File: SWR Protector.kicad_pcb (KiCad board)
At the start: 2 copper layers, 82.7 x 56.6 mm, 28 parts, among them J1 Barrel_Jack, J2 Barrel_Jack, J3 transceiver, J4 antenna, J5 header, K2 ATX209, Q1 2N3904, T1 1:12, T2 1:12, U1 LM78L05_TO92, U2 LM358

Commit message: checkpoint changes working on V2.0
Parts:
- moved J1 1.63 mm to (182.6, 124.5)
- moved J2 1.02 mm to (127.3, 124.5)
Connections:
- U2 pad 8: +5V -> +12V
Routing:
- net +12V: track 54.2 -> 72.9 mm
- net +5V: track 124.4 -> 108.5 mm
- net GND: vias 74 -> 0

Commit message: checkpoint changes working on V2.0
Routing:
- net +5V: track 108.5 -> 117.7 mm, vias 2 -> 1
- net Net-(D4-K): track 47.2 -> 48.6 mm
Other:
- board text added: "SWR Protector v1.1"
- board text removed: "SWR Protector v1.0"

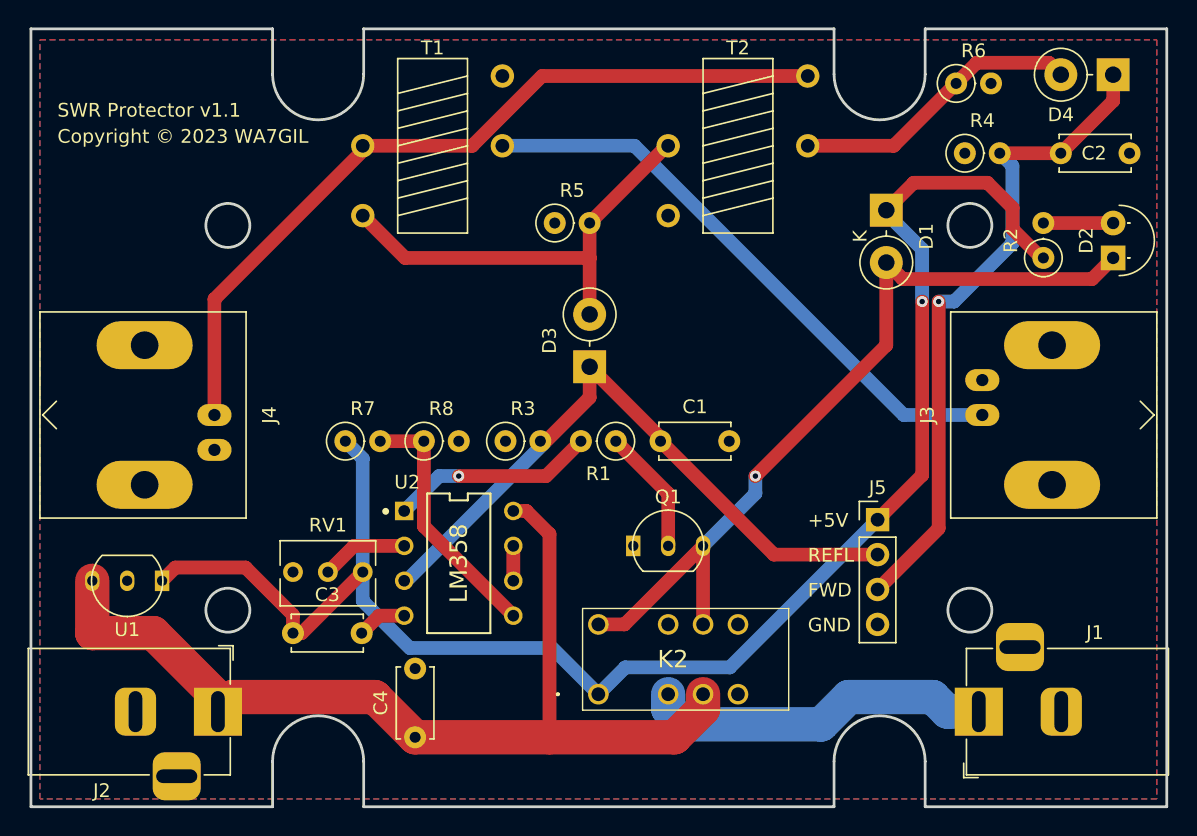
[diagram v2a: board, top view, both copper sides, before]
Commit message: completed everything on the list of requested changes in V2-Changelog.txt.  Passes DRC, but we get warnings for things like silkscreen off the edge of the board (deliberate, for the power connectors).  Needs a hard squint, then send it off to the fab.
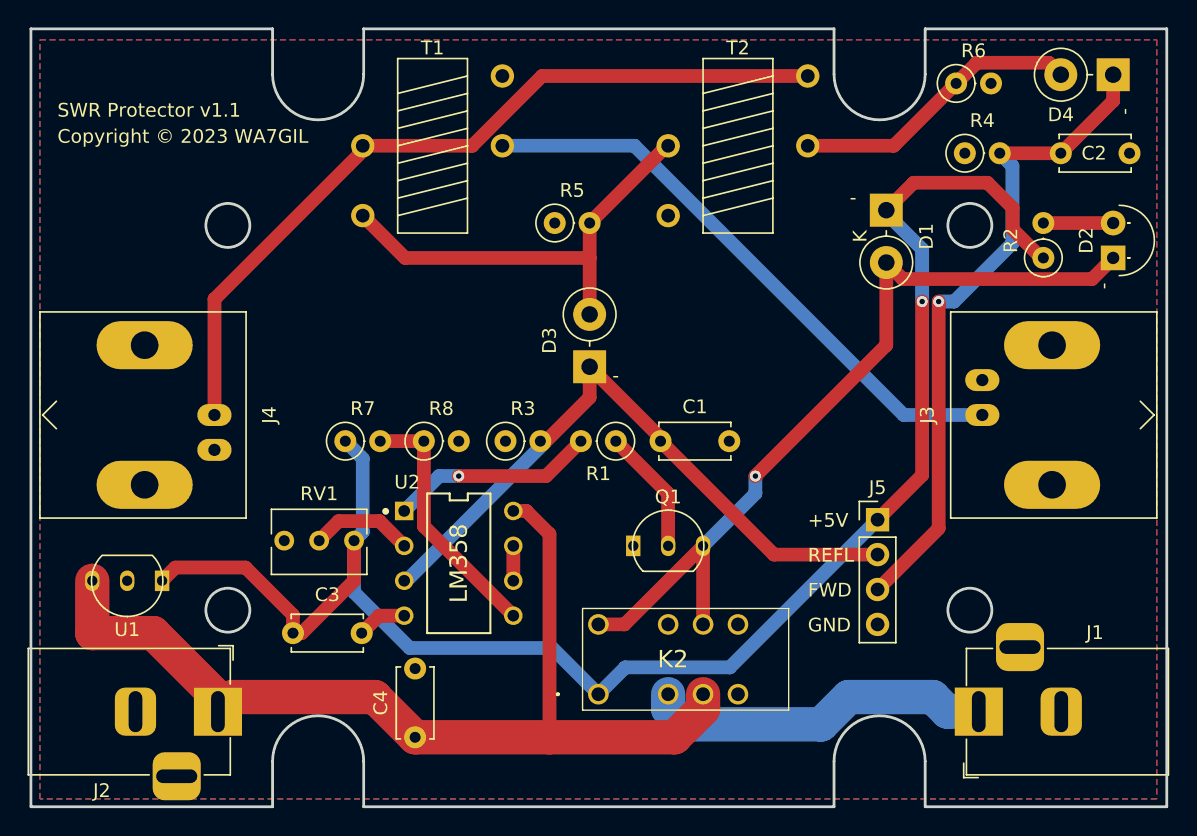
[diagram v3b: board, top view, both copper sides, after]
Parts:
- moved RV1 2.37 mm to (137.2, 112.0)
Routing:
- net +5V: track 117.7 -> 120.2 mm
- net Net-(U2A--): track 6.34 -> 7.52 mm
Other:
- board text added: "-"
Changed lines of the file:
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@@
   )
   (footprint "Potentiometer_THT:Potentiometer_Bourns_3266Y_Vertical" (layer "F.Cu")
-    (at 137.795 114.3)
+    (at 137.16 112.014)
     (descr "Potentiometer, vertical, Bourns 3266Y, https://www.bourns.com/docs/Product-Datasheets/3266.pdf")
     (tags "Potentiometer vertical Bourns 3266Y")
@@
     (fp_line (start 0.935 0.496) (end 0.935 2.46)
       (stroke (width 0.12) (type solid)) (layer "F.SilkS"))
-    (fp_line (start -6.15 -2.45) (end -6.15 2.6)
-      (stroke (width 0.05) (type solid)) (layer "F.CrtYd"))
-    (fp_line (start -6.15 2.6) (end 1.1 2.6)
-      (stroke (width 0.05) (type solid)) (layer "F.CrtYd"))
-    (fp_line (start 1.1 -2.45) (end -6.15 -2.45)
-      (stroke (width 0.05) (type solid)) (layer "F.CrtYd"))
-    (fp_line (start 1.1 2.6) (end 1.1 -2.45)
+    (fp_line (start -7 -4.5) (end -7 4.5)
+      (stroke (width 0.05) (type solid)) (layer "F.CrtYd"))
+    (fp_line (start -7 4.5) (end 2 4.5)
+      (stroke (width 0.05) (type solid)) (layer "F.CrtYd"))
+    (fp_line (start 2 -4.5) (end -7 -4.5)
+      (stroke (width 0.05) (type solid)) (layer "F.CrtYd"))
+    (fp_line (start 2 4.5) (end 2 -4.5)
       (stroke (width 0.05) (type solid)) (layer "F.CrtYd"))
     (fp_line (start -5.895 -2.16) (end -5.895 2.34)
@@
     (effects (font (size 1 1) (thickness 0.15)) (justify left bottom))
   )
+  (gr_text "-" (at 193.802 81.026 90) (layer "F.SilkS")
+    (effects (font (size 1 1) (thickness 0.15)) (justify left bottom))
+  )
+  (gr_text "-" (at 192.278 93.726 90) (layer "F.SilkS")
+    (effects (font (size 1 1) (thickness 0.15)) (justify left bottom))
+  )
+  (gr_text "-" (at 173.228 87.63) (layer "F.SilkS")
+    (effects (font (size 1 1) (thickness 0.15)) (justify left bottom))
+  )
   (gr_text "REFL" (at 170.18 113.665) (layer "F.SilkS")
     (effects (font (size 1 1) (thickness 0.15)) (justify left bottom))
@@
   )
   (gr_text "SWR Protector v1.1" (at 115.57 81.28) (layer "F.SilkS")
+    (effects (font (size 1 1) (thickness 0.15)) (justify left bottom))
+  )
+  (gr_text "-" (at 155.956 100.584) (layer "F.SilkS")
     (effects (font (size 1 1) (thickness 0.15)) (justify left bottom))
   )
@@
   (segment (start 185.076693 84.746693) (end 185.076693 90.362295) (width 1) (layer "B.Cu") (net 3))
   (segment (start 184.15 83.82) (end 185.076693 84.746693) (width 1) (layer "B.Cu") (net 3))
-  (segment (start 132.715 118.745) (end 133.35 118.745) (width 1) (layer "F.Cu") (net 4))
   (segment (start 185.08705 87.797784) (end 183.261593 85.972327) (width 1) (layer "F.Cu") (net 4))
   (segment (start 132.715 117.425734) (end 129.261593 113.972327) (width 1) (layer "F.Cu") (net 4))
+  (segment (start 132.715 118.745) (end 133.35 118.745) (width 1) (layer "F.Cu") (net 4))
   (segment (start 124.152673 113.972327) (end 123.19 114.935) (width 1) (layer "F.Cu") (net 4))
+  (segment (start 133.35 118.745) (end 137.16 114.935) (width 1) (layer "F.Cu") (net 4))
   (segment (start 185.08705 89.344041) (end 185.08705 87.797784) (width 1) (layer "F.Cu") (net 4))
   (segment (start 177.887673 85.972327) (end 175.895 87.965) (width 1) (layer "F.Cu") (net 4))
   (segment (start 187.325 91.44) (end 187.183009 91.44) (width 1) (layer "F.Cu") (net 4))
-  (segment (start 133.35 118.745) (end 137.795 114.3) (width 1) (layer "F.Cu") (net 4))
   (segment (start 178.505 107.245) (end 178.505 94.615) (width 1) (layer "F.Cu") (net 4))
   (segment (start 187.183009 91.44) (end 185.08705 89.344041) (width 1) (layer "F.Cu") (net 4))
@@
   (segment (start 183.261593 85.972327) (end 177.887673 85.972327) (width 1) (layer "F.Cu") (net 4))
   (segment (start 129.261593 113.972327) (end 124.152673 113.972327) (width 1) (layer "F.Cu") (net 4))
+  (segment (start 137.16 114.935) (end 137.16 112.014) (width 1) (layer "F.Cu") (net 4))
   (via (at 178.505 94.615) (size 0.8) (drill 0.4) (layers "F.Cu" "B.Cu") (net 4))
+  (segment (start 141.215456 119.825) (end 151.575 119.825) (width 1) (layer "B.Cu") (net 4))
   (segment (start 175.895 88.195) (end 178.505 90.805) (width 1) (layer "B.Cu") (net 4))
-  (segment (start 141.215456 119.825) (end 151.575 119.825) (width 1) (layer "B.Cu") (net 4))
   (segment (start 175.26 110.49) (end 164.51 121.24) (width 1) (layer "B.Cu") (net 4))
   (segment (start 178.505 94.615) (end 178.505 90.805) (width 1) (layer "B.Cu") (net 4))
-  (segment (start 137.795 114.3) (end 137.795 116.404544) (width 1) (layer "B.Cu") (net 4))
+  (segment (start 151.575 119.825) (end 154.94 123.19) (width 1) (layer "B.Cu") (net 4))
   (segment (start 156.89 121.24) (end 154.94 123.19) (width 1) (layer "B.Cu") (net 4))
   (segment (start 164.51 121.24) (end 156.89 121.24) (width 1) (layer "B.Cu") (net 4))
+  (segment (start 137.795 111.379) (end 137.795 106.045) (width 1) (layer "B.Cu") (net 4))
+  (segment (start 175.895 87.965) (end 175.895 88.195) (width 1) (layer "B.Cu") (net 4))
+  (segment (start 137.16 112.014) (end 137.795 111.379) (width 1) (layer "B.Cu") (net 4))
+  (segment (start 137.16 112.014) (end 137.16 115.769544) (width 1) (layer "B.Cu") (net 4))
+  (segment (start 137.16 115.769544) (end 141.215456 119.825) (width 1) (layer "B.Cu") (net 4))
   (segment (start 137.795 106.045) (end 136.525 104.775) (width 1) (layer "B.Cu") (net 4))
-  (segment (start 175.895 87.965) (end 175.895 88.195) (width 1) (layer "B.Cu") (net 4))
-  (segment (start 137.795 116.404544) (end 141.215456 119.825) (width 1) (layer "B.Cu") (net 4))
-  (segment (start 151.575 119.825) (end 154.94 123.19) (width 1) (layer "B.Cu") (net 4))
-  (segment (start 137.795 114.3) (end 137.795 106.045) (width 1) (layer "B.Cu") (net 4))
   (segment (start 122.555 118.745) (end 118.11 118.745) (width 2.5) (layer "F.Cu") (net 5))
   (segment (start 151.384 111.534406) (end 151.384 126.325) (width 1) (layer "F.Cu") (net 5))
@@
   (segment (start 142.24 104.775) (end 139.065 104.775) (width 1) (layer "F.Cu") (net 17))
   (segment (start 142.24 110.965) (end 148.75 117.475) (width 1) (layer "F.Cu") (net 17))
-  (segment (start 140.81 112.395) (end 137.16 112.395) (width 1) (layer "F.Cu") (net 18))
-  (segment (start 137.16 112.395) (end 135.255 114.3) (width 1) (layer "F.Cu") (net 18))
+  (segment (start 139.009 110.594) (end 140.81 112.395) (width 1) (layer "F.Cu") (net 18))
+  (segment (start 136.04 110.594) (end 139.009 110.594) (width 1) (layer "F.Cu") (net 18))
+  (segment (start 134.62 112.014) (end 136.04 110.594) (width 1) (layer "F.Cu") (net 18))
   (segment (start 148.75 114.935) (end 148.75 112.395) (width 1) (layer "F.Cu") (net 19))
   (zone (net 2) (net_name "GND") (layer "F.Cu") (hatch edge 0.5)

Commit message: v1.2 - added pins 2 & 3 from LM358 to header
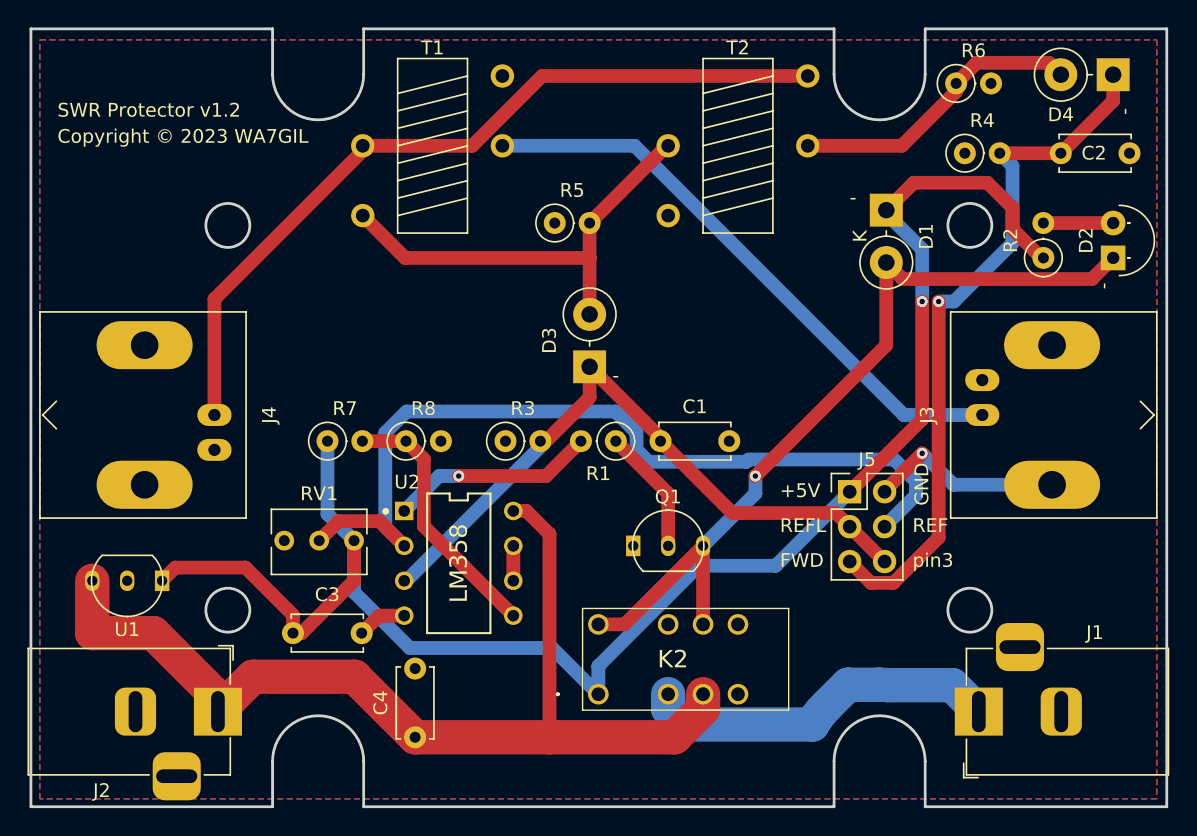
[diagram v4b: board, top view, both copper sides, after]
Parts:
- J5: value header -> Conn_02x03; footprint Connector_PinHeader_2.54mm:PinHeader_1x04_P2.54mm_Vertical -> Connector_PinHeader_2.54mm:PinHeader_2x03_P2.54mm_Vertical
- moved J5 2.87 mm to (173.2, 108.5)
- moved R7 1.30 mm to (135.2, 104.8)
- moved R8 1.30 mm to (140.9, 104.8)
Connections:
- J5 pad 2: Net-(D3-K) -> GND
- J5 pad 3: Net-(D4-K) -> Net-(D3-K)
- J5 pad 4: GND -> Net-(J5-Pin_4)
- RV1 pad 2: Net-(U2A--) -> Net-(J5-Pin_4)
- U2 pad 2: Net-(U2A--) -> Net-(J5-Pin_4)
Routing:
- net Net-(J5-Pin_4): track 0.00 -> 62.8 mm
- net GND: track 3.62 -> 18.0 mm, vias 0 -> 1
- net Net-(U2A--): track 7.52 -> 0.00 mm
- net Net-(D4-K): track 48.6 -> 51.5 mm
- net +12V: track 72.9 -> 74.1 mm
- net +5V: track 120.2 -> 119.0 mm
- net Net-(K2-NC_1): track 25.4 -> 26.3 mm
- net Net-(D3-K): track 48.0 -> 48.7 mm
- net Net-(U2B-+): track 18.6 -> 19.1 mm
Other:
- board text added: "REF"
- board text added: "SWR Protector v1.2"
- board text added: "pin3"
- board text removed: "SWR Protector v1.1"

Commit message: checkpoint changes made late satuday that i cannot remember what i did
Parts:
- renumbered C4 to C2, C2 to C4, D3 to D1, D4 to D2, D2 to D3, D1 to D4, J2 to J1, J4 to J2, J5 to J3, J3 to J4, J1 to J5, K2 to K1, R5 to R1, R3 to R2, R4 to R3, R6 to R4, R1 to R5, R2 to R6

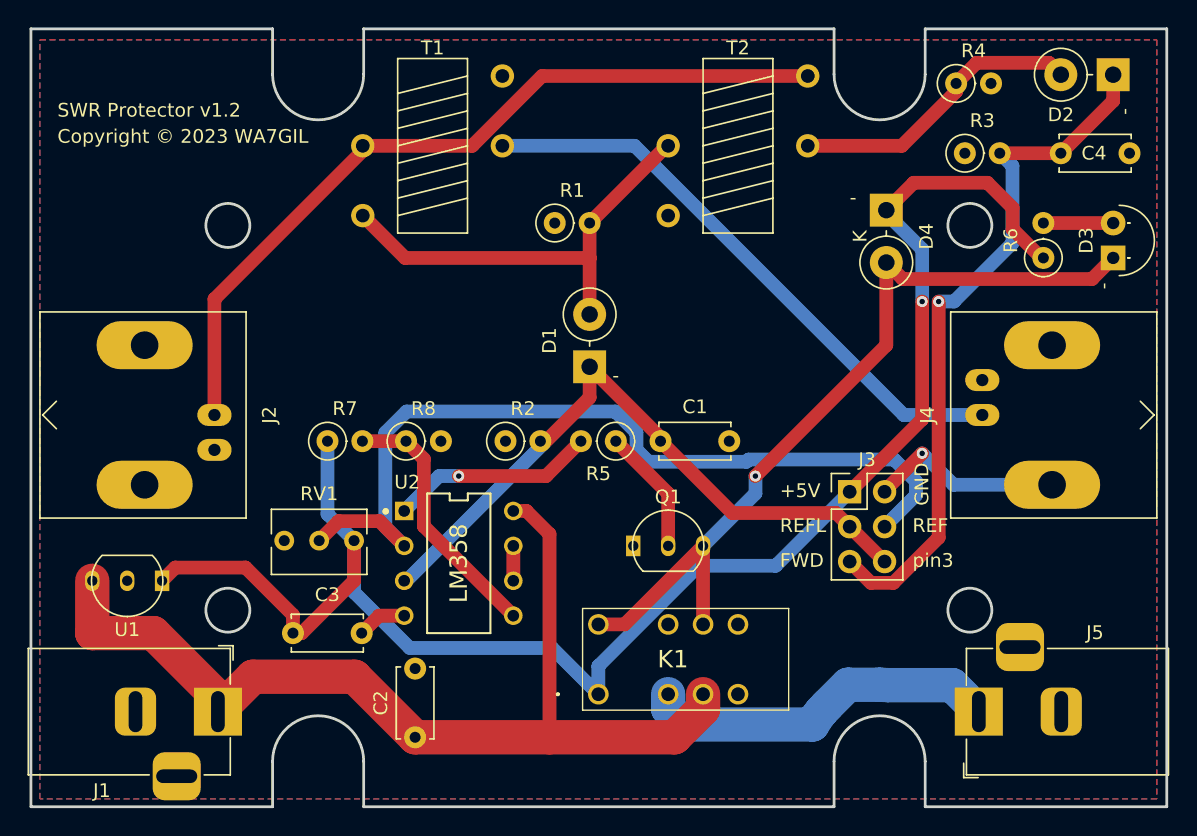
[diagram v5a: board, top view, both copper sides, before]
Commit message: Removed pin 6 on header.  Fine tune footprint for Q1. Realizing pin 6 on header just duplicated the VReflected voltage already on pin 3, I made pin 6 NC. Fiddled with footprint for Q1 to try to remove "Silkscreen clipped by solder mask" warnings.
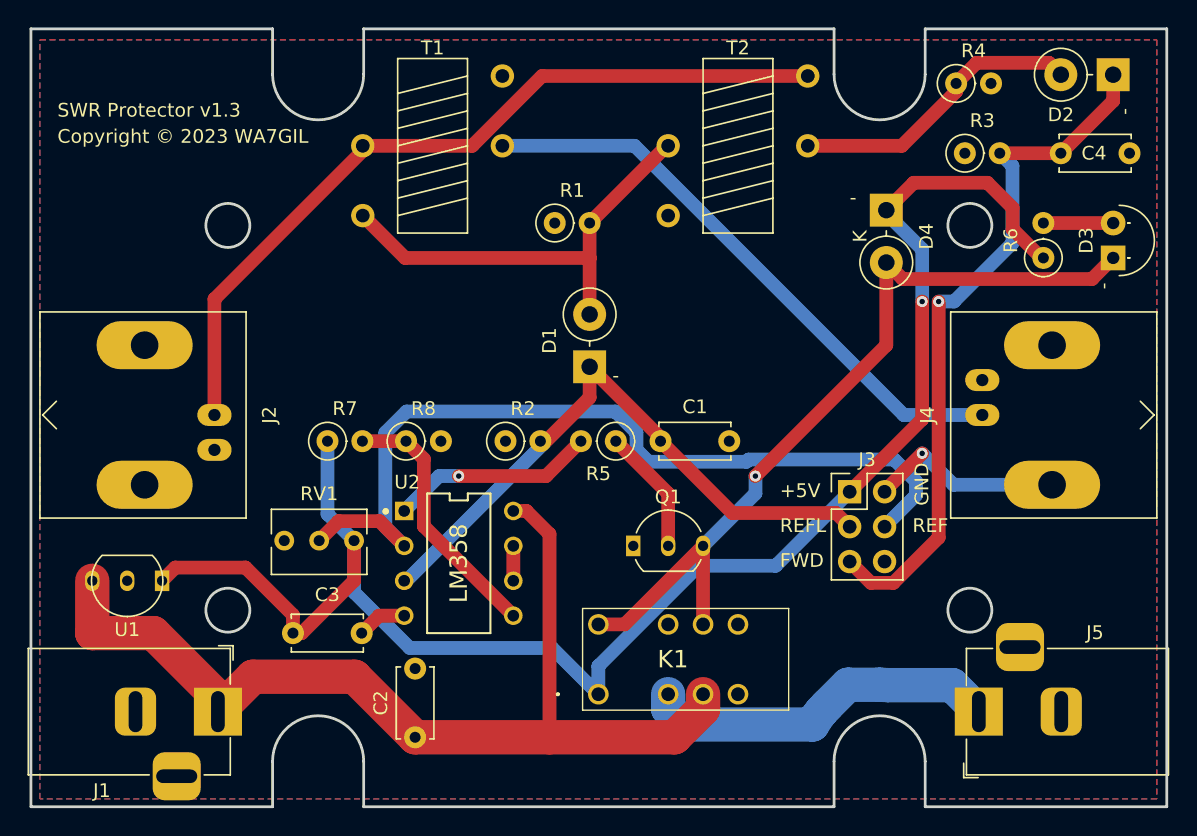
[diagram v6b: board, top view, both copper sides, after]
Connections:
- J3 pad 6: Net-(D1-K) -> unconnected-(J3-Pin_6-Pad6)
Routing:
- net Net-(D1-K): track 48.7 -> 45.2 mm
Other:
- board text added: "SWR Protector v1.3"
- board text removed: "SWR Protector v1.2"
- board text removed: "pin3"
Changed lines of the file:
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@@
   (title_block
     (title "SWR Protector WA7GIL")
-    (date "2023-05-27")
-    (rev "v1.2")
+    (date "2023-05-28")
+    (rev "v1.3")
   )
   (layers
@@
   (net 18 "Net-(R5-Pad2)")
   (net 19 "Net-(U2B--)")
+  (net 20 "unconnected-(J3-Pin_6-Pad6)")
   (footprint "Capacitor_THT:C_Disc_D5.0mm_W2.5mm_P5.00mm" (layer "F.Cu")
     (at 188.595 83.82)
@@
     (fp_line (start -0.53 1.85) (end 3.07 1.85)
       (stroke (width 0.12) (type solid)) (layer "F.SilkS"))
-    (fp_arc (start -0.568478 1.838478) (mid -1.132087 -0.994977) (end 1.27 -2.6)
-      (stroke (width 0.12) (type solid)) (layer "F.SilkS"))
-    (fp_arc (start 1.27 -2.6) (mid 3.672087 -0.994977) (end 3.108478 1.838478)
+    (fp_arc (start -1.045667 -0.95) (mid -0.146539 -2.141603) (end 1.269762 -2.613235)
+      (stroke (width 0.12) (type solid)) (layer "F.SilkS"))
+    (fp_arc (start -0.573696 1.80132) (mid -0.874247 1.425223) (end -1.1 1)
+      (stroke (width 0.12) (type solid)) (layer "F.SilkS"))
+    (fp_arc (start 1.27 -2.601326) (mid 2.690476 -2.179253) (end 3.649999 -1.05)
+      (stroke (width 0.12) (type solid)) (layer "F.SilkS"))
+    (fp_arc (start 3.649999 1) (mid 3.412643 1.4356) (end 3.096913 1.818222)
       (stroke (width 0.12) (type solid)) (layer "F.SilkS"))
     (fp_line (start -1.46 -2.73) (end -1.46 2.01)
@@
       (net 9 "Net-(D2-K)") (pinfunction "Pin_5") (pintype "passive"))
     (pad "6" thru_hole oval (at 2.54 5.08) (size 1.7 1.7) (drill 1) (layers "*.Cu" "*.Mask")
-      (net 3 "Net-(D1-K)") (pinfunction "Pin_6") (pintype "passive"))
+      (net 20 "unconnected-(J3-Pin_6-Pad6)") (pinfunction "Pin_6") (pintype "no_connect"))
     (model "${KICAD6_3DMODEL_DIR}/Connector_PinHeader_2.54mm.3dshapes/PinHeader_2x03_P2.54mm_Vertical.wrl"
       (offset (xyz 0 0 0))
@@
     (effects (font (size 1.5 1.5) (thickness 0.3) bold) (justify left bottom mirror))
   )
-  (gr_text "pin3" (at 177.8 114.046) (layer "F.SilkS")
-    (effects (font (size 1 1) (thickness 0.15)) (justify left bottom))
-  )
   (gr_text "-" (at 193.802 81.026 90) (layer "F.SilkS")
     (effects (font (size 1 1) (thickness 0.15)) (justify left bottom))
@@
     (effects (font (size 1 1) (thickness 0.15)) (justify left bottom))
   )
-  (gr_text "SWR Protector v1.2" (at 115.57 81.28) (layer "F.SilkS")
+  (gr_text "SWR Protector v1.3" (at 115.57 81.28) (layer "F.SilkS")
     (effects (font (size 1 1) (thickness 0.15)) (justify left bottom))
   )
@@
   (segment (start 154.305 101.6) (end 151.13 104.775) (width 1) (layer "F.Cu") (net 3))
   (segment (start 159.465 104.775) (end 159.465 104.52) (width 1) (layer "F.Cu") (net 3))
-  (segment (start 172.238 110.008) (end 175.768 113.538) (width 1) (layer "F.Cu") (net 3))
+  (segment (start 173.228 110.998) (end 172.238 110.008) (width 1) (layer "F.Cu") (net 3))
   (segment (start 159.465 104.775) (end 164.698 110.008) (width 1) (layer "F.Cu") (net 3))
   (segment (start 151.13 104.775) (end 140.97 114.935) (width 1) (layer "B.Cu") (net 3))
